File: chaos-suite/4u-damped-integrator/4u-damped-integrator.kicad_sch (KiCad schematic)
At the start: 56 parts

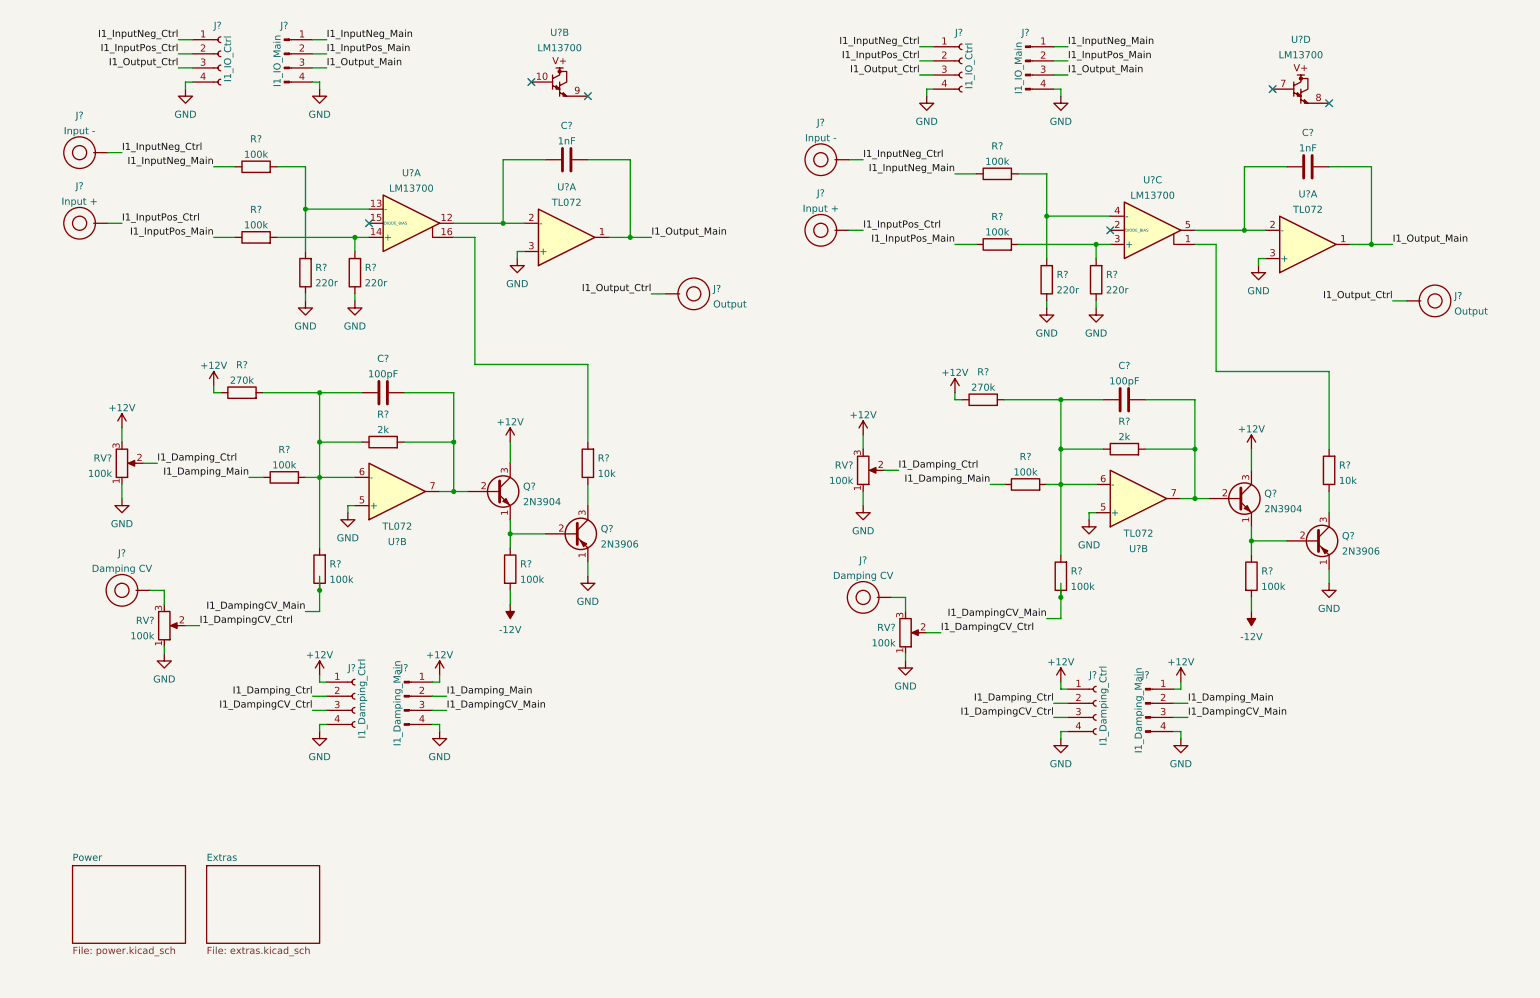
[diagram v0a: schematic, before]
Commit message: Laying out damped integrator pcb
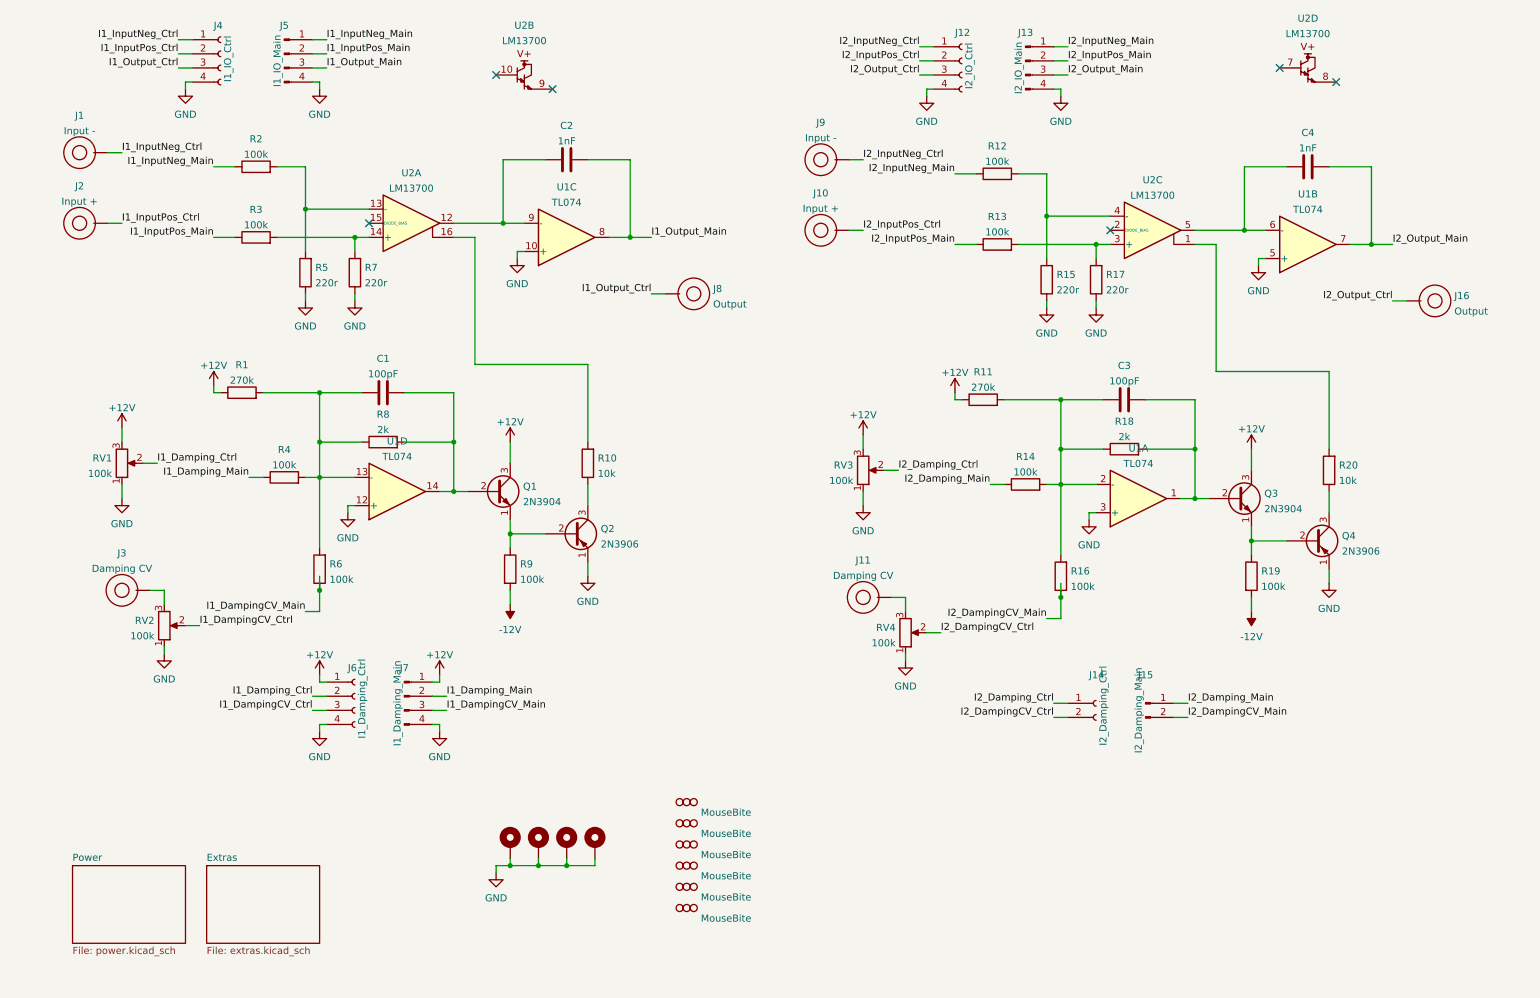
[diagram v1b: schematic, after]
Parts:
- removed U? (x4): TL072, symbol Amplifier_Operational:TL072
- added H1, H2, H3, H4: MountingHole_Pad, MountingHole:MountingHole_3.2mm_M3_DIN965_Pad, symbol Mechanical:MountingHole_Pad
- added H10, H5, H6, H7, H8, H9: MouseBite, Panelization:mouse-bite-2mm-slot, symbol Panelization:MouseBite
- added U1: TL074, Rumblesan_Footprints:DIP-14_W7.62mm_Socket, symbol Amplifier_Operational:TL074
- C1, C2, C3, C4: renamed from C?; footprint (none) -> Rumblesan_Footprints:C_Rect_L7.0mm_W3.5mm_P5.00mm
- J1, J10, J11, J16, J2, J3, J8, J9: renamed from J?; footprint (none) -> Rumblesan_Footprints:BananaJack_THT_JohnsonCinch_108-09
- J12: renamed from J?; value I1_IO_Ctrl -> I2_IO_Ctrl; footprint (none) -> Connector_PinSocket_2.54mm:PinSocket_1x04_P2.54mm_Vertical
- J13: renamed from J?; value I1_IO_Main -> I2_IO_Main; footprint (none) -> Connector_PinHeader_2.54mm:PinHeader_1x04_P2.54mm_Vertical
- J14: renamed from J?; value I1_Damping_Ctrl -> I2_Damping_Ctrl; footprint (none) -> Connector_PinSocket_2.54mm:PinSocket_1x02_P2.54mm_Vertical; symbol Connector:Conn_01x04_Female -> Connector:Conn_01x02_Female
- J15: renamed from J?; value I1_Damping_Main -> I2_Damping_Main; footprint (none) -> Connector_PinHeader_2.54mm:PinHeader_1x02_P2.54mm_Vertical; symbol Connector:Conn_01x04_Male -> Connector:Conn_01x02_Male
- J4, J6: renamed from J?; footprint (none) -> Connector_PinSocket_2.54mm:PinSocket_1x04_P2.54mm_Vertical
- J5, J7: renamed from J?; footprint (none) -> Connector_PinHeader_2.54mm:PinHeader_1x04_P2.54mm_Vertical
- Q1, Q2, Q3, Q4: renamed from Q?; footprint Package_TO_SOT_THT:TO-92_Inline -> Package_TO_SOT_THT:TO-92_Inline_Wide
- R1, R10, R11, R12, R13, R14, R15, R16, R17, R18, R19, R2, R20, R3, R4, R5, R6, R7, R8, R9: renamed from R?; footprint (none) -> Rumblesan_Footprints:Resistor_THT_L6.3mm_D2.5mm_P10.16mm_Horizontal
- RV1, RV2, RV3, RV4: renamed from RV?; footprint (none) -> Rumblesan_Footprints:Potentiometer_Alpha_RD901F-40-00D_Single_Vertical_CircularHoles
- U2: renamed from U?; footprint (none) -> Rumblesan_Footprints:DIP-16_W7.62mm_Socket
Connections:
- net +12V: no longer J14.1 (Pin_1), J15.1 (Pin_1)
- net GND: now also H1.1, H2.1, H3.1, H4.1, U1.10 (+), U1.12 (+), U1.3 (+), U1.5 (+); no longer J14.4 (Pin_4), J15.4 (Pin_4)
- net I1_DampingCV_Ctrl: no longer J14.3 (Pin_3), RV4.2
- net I1_DampingCV_Main: no longer J15.3 (Pin_3), R16.1
- net I1_Damping_Ctrl: no longer J14.2 (Pin_2), RV3.2
- net I1_Damping_Main: no longer J15.2 (Pin_2), R14.1
- net I1_InputNeg_Ctrl: no longer J12.1 (Pin_1), J9.1
- net I1_InputNeg_Main: no longer J13.1 (Pin_1), R12.1
- net I1_InputPos_Ctrl: no longer J10.1, J12.2 (Pin_2)
- net I1_InputPos_Main: no longer J13.2 (Pin_2), R13.1
- net I1_Output_Ctrl: no longer J12.3 (Pin_3), J16.1
- net I1_Output_Main: now also U1.8; no longer C4.2, J13.3 (Pin_3)
- net at C2.1, U2.12: now also U1.9 (-)
- net at C1.1, R1.2, R4.2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: now also U1.13 (-)
- net at C1.2, Q1.2 (B), R8.2: now also U1.14
- net at C3.1, R11.2, R14.2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: now also U1.2 (-)
- net at C3.2, Q3.2 (B), R18.2: now also U1.1
- net at C4.1, U2.5: now also U1.6 (-)
- new net I2_DampingCV_Ctrl: J14.2 (Pin_2), RV4.2
- new net I2_DampingCV_Main: J15.2 (Pin_2), R16.1
- new net I2_Damping_Ctrl: J14.1 (Pin_1), RV3.2
- new net I2_Damping_Main: J15.1 (Pin_1), R14.1
- new net I2_InputNeg_Ctrl: J12.1 (Pin_1), J9.1
- new net I2_InputNeg_Main: J13.1 (Pin_1), R12.1
- new net I2_InputPos_Ctrl: J10.1, J12.2 (Pin_2)
- new net I2_InputPos_Main: J13.2 (Pin_2), R13.1
- new net I2_Output_Ctrl: J12.3 (Pin_3), J16.1
- new net I2_Output_Main: C4.2, J13.3 (Pin_3), U1.7
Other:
- moved on the sheet: U2B, U2D

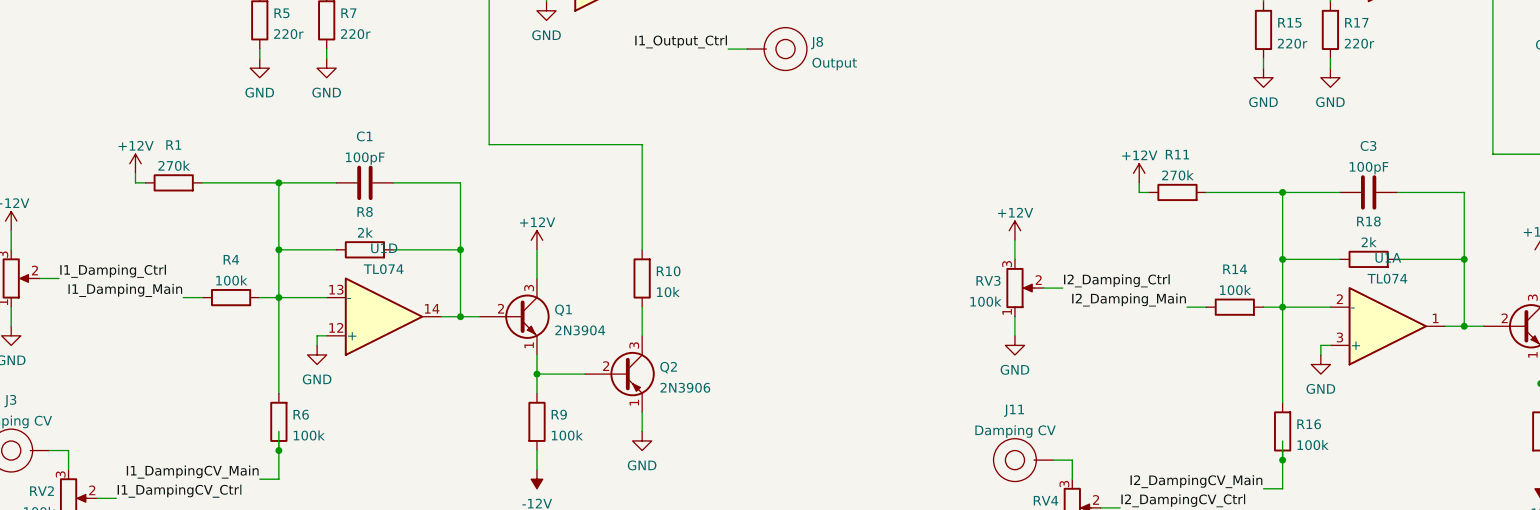
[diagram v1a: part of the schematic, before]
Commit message: final damped integrator tweaks
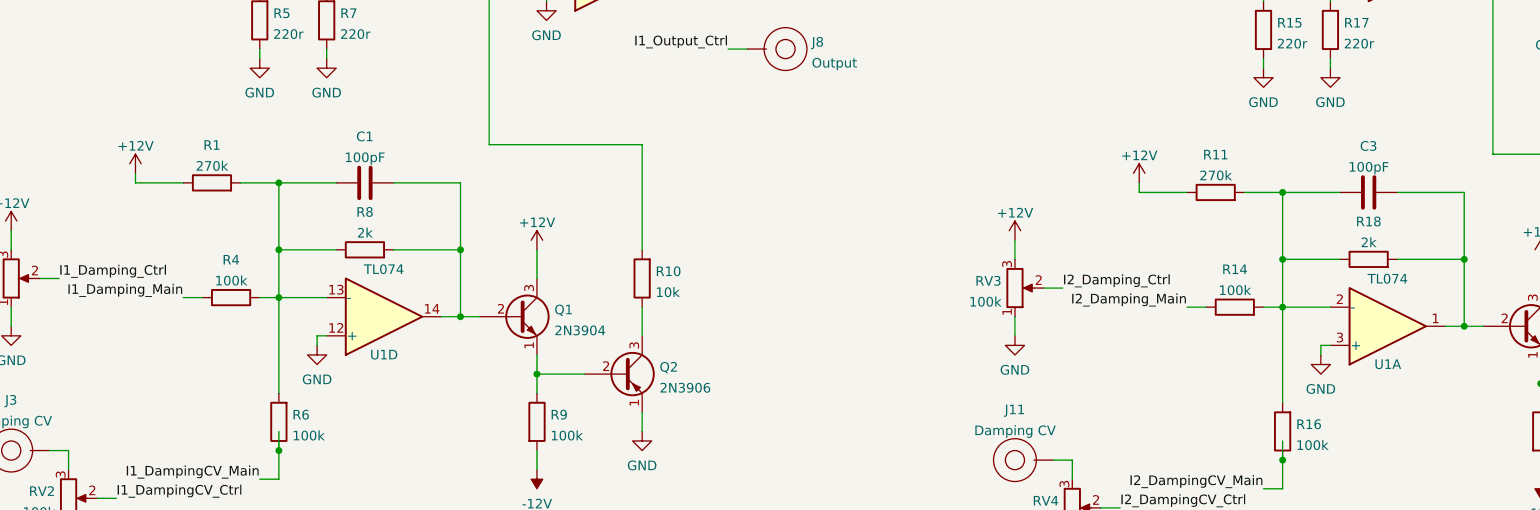
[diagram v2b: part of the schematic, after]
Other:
- title: (none) -> Damped Integrator
- moved on the sheet: R1, R11
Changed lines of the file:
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@@
 (kicad_sch (version 20211123) (generator eeschema)
   (paper "A4")
+  (title_block
+    (title "Damped Integrator")
+    (date "2022-06-17")
+    (rev "r01")
+    (comment 2 "creativecommons.org/Licenses/by/4.0/")
+    (comment 3 "License: CC BY 4.0")
+    (comment 4 "Author: Guy John")
+  )
   (junction (at 69.85 96.52) (diameter 0) (color 0 0 0 0)
   )
@@
     (stroke (width 0) (type default) (color 0 0 0 0))
   )
-  (wire (pts (xy 184.15 88.9) (xy 185.42 88.9))
+  (wire (pts (xy 184.15 88.9) (xy 190.5 88.9))
     (stroke (width 0) (type default) (color 0 0 0 0))
   )
@@
     (stroke (width 0) (type default) (color 0 0 0 0))
   )
-  (wire (pts (xy 193.04 88.9) (xy 203.2 88.9))
+  (wire (pts (xy 198.12 88.9) (xy 203.2 88.9))
     (stroke (width 0) (type default) (color 0 0 0 0))
   )
@@
     (stroke (width 0) (type default) (color 0 0 0 0))
   )
-  (wire (pts (xy 59.69 87.63) (xy 69.85 87.63))
+  (wire (pts (xy 64.77 87.63) (xy 69.85 87.63))
     (stroke (width 0) (type default) (color 0 0 0 0))
   )
@@
     (stroke (width 0) (type default) (color 0 0 0 0))
   )
-  (wire (pts (xy 50.8 87.63) (xy 52.07 87.63))
+  (wire (pts (xy 50.8 87.63) (xy 57.15 87.63))
     (stroke (width 0) (type default) (color 0 0 0 0))
   )
@@
   )
   (symbol (lib_id "Amplifier_Operational:TL074") (at 217.17 106.68 0) (mirror x) (unit 1)
-    (in_bom yes) (on_board yes) (fields_autoplaced)
-    (property "Reference" "U1" (id 0) (at 217.17 97.6335 0))
+    (in_bom yes) (on_board yes)
+    (property "Reference" "U1" (id 0) (at 217.17 111.76 0))
     (property "Value" "TL074" (id 1) (at 217.17 100.4086 0))
     (property "Footprint" "Rumblesan_Footprints:DIP-14_W7.62mm_Socket" (id 2) (at 215.9 109.22 0)
@@
     )
   )
-  (symbol (lib_id "Device:R") (at 189.23 88.9 90) (unit 1)
-    (in_bom yes) (on_board yes) (fields_autoplaced)
-    (property "Reference" "R11" (id 0) (at 189.23 83.9175 90))
-    (property "Value" "270k" (id 1) (at 189.23 86.6926 90))
-    (property "Footprint" "Rumblesan_Footprints:Resistor_THT_L6.3mm_D2.5mm_P10.16mm_Horizontal" (id 2) (at 189.23 90.678 90)
-      (effects (font (size 1.27 1.27)) hide)
-    )
-    (property "Datasheet" "~" (id 3) (at 189.23 88.9 0)
+  (symbol (lib_id "Device:R") (at 194.31 88.9 90) (unit 1)
+    (in_bom yes) (on_board yes) (fields_autoplaced)
+    (property "Reference" "R11" (id 0) (at 194.31 83.9175 90))
+    (property "Value" "270k" (id 1) (at 194.31 86.6926 90))
+    (property "Footprint" "Rumblesan_Footprints:Resistor_THT_L6.3mm_D2.5mm_P10.16mm_Horizontal" (id 2) (at 194.31 90.678 90)
+      (effects (font (size 1.27 1.27)) hide)
+    )
+    (property "Datasheet" "~" (id 3) (at 194.31 88.9 0)
       (effects (font (size 1.27 1.27)) hide)
     )
@@
   )
   (symbol (lib_id "Amplifier_Operational:TL074") (at 83.82 105.41 0) (mirror x) (unit 4)
-    (in_bom yes) (on_board yes) (fields_autoplaced)
-    (property "Reference" "U1" (id 0) (at 83.82 96.3635 0))
+    (in_bom yes) (on_board yes)
+    (property "Reference" "U1" (id 0) (at 83.82 110.49 0))
     (property "Value" "TL074" (id 1) (at 83.82 99.1386 0))
     (property "Footprint" "Rumblesan_Footprints:DIP-14_W7.62mm_Socket" (id 2) (at 82.55 107.95 0)
@@
     (pin "1")
   )
-  (symbol (lib_id "Device:R") (at 55.88 87.63 90) (unit 1)
-    (in_bom yes) (on_board yes) (fields_autoplaced)
-    (property "Reference" "R1" (id 0) (at 55.88 82.6475 90))
-    (property "Value" "270k" (id 1) (at 55.88 85.4226 90))
-    (property "Footprint" "Rumblesan_Footprints:Resistor_THT_L6.3mm_D2.5mm_P10.16mm_Horizontal" (id 2) (at 55.88 89.408 90)
-      (effects (font (size 1.27 1.27)) hide)
-    )
-    (property "Datasheet" "~" (id 3) (at 55.88 87.63 0)
-      (effects (font (size 1.27 1.27)) hide)
-    )
+  (symbol (lib_id "Device:R") (at 60.96 87.63 90) (unit 1)
+    (in_bom yes) (on_board yes) (fields_autoplaced)
+    (property "Reference" "R1" (id 0) (at 60.96 82.6475 90))
+    (property "Value" "270k" (id 1) (at 60.96 85.4226 90))
+    (property "Footprint" "Rumblesan_Footprints:Resistor_THT_L6.3mm_D2.5mm_P10.16mm_Horizontal" (id 2) (at 60.96 89.408 90)
+      (effects (font (size 1.27 1.27)) hide)
+    )
+    (property "Datasheet" "~" (id 3) (at 60.96 87.63 0)
+      (effects (font (size 1.27 1.27)) hide)
+    )
